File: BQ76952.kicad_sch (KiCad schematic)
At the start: 1 part, among them U3 BQ76952PFBR

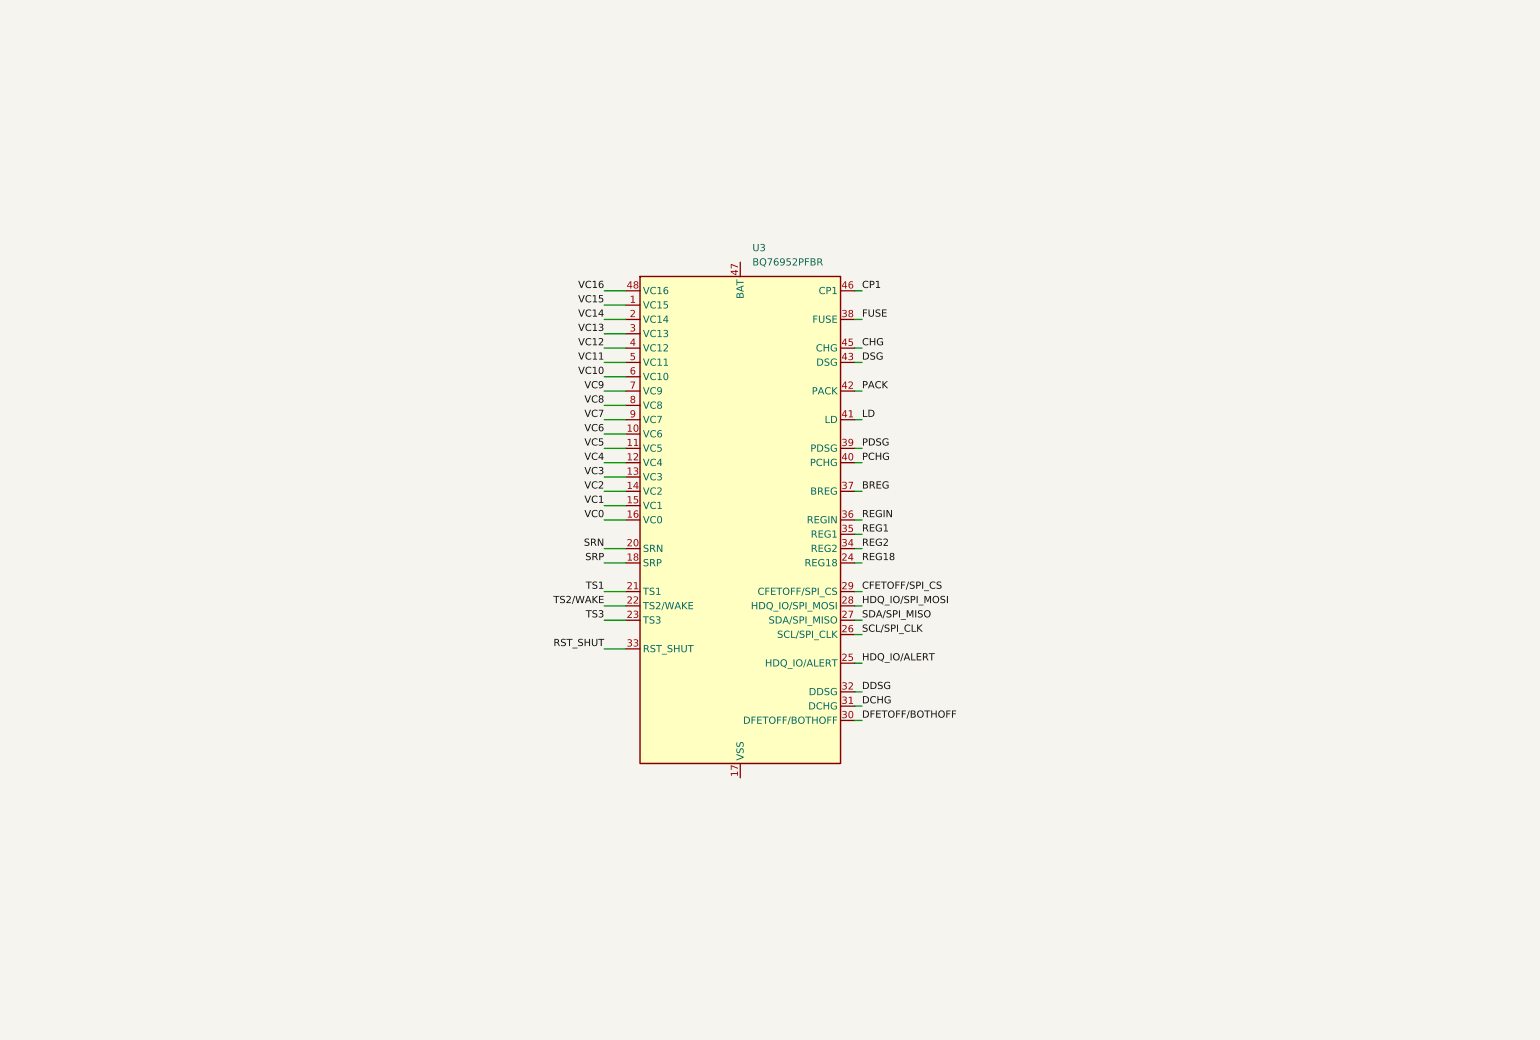
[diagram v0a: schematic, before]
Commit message: Add files via upload
Updated BQ76952 schematic with passive cell balancing, voltage readout to ESP32 and temperature sensing. To do: Connect remaining pins on BQ76952 to ESP32.
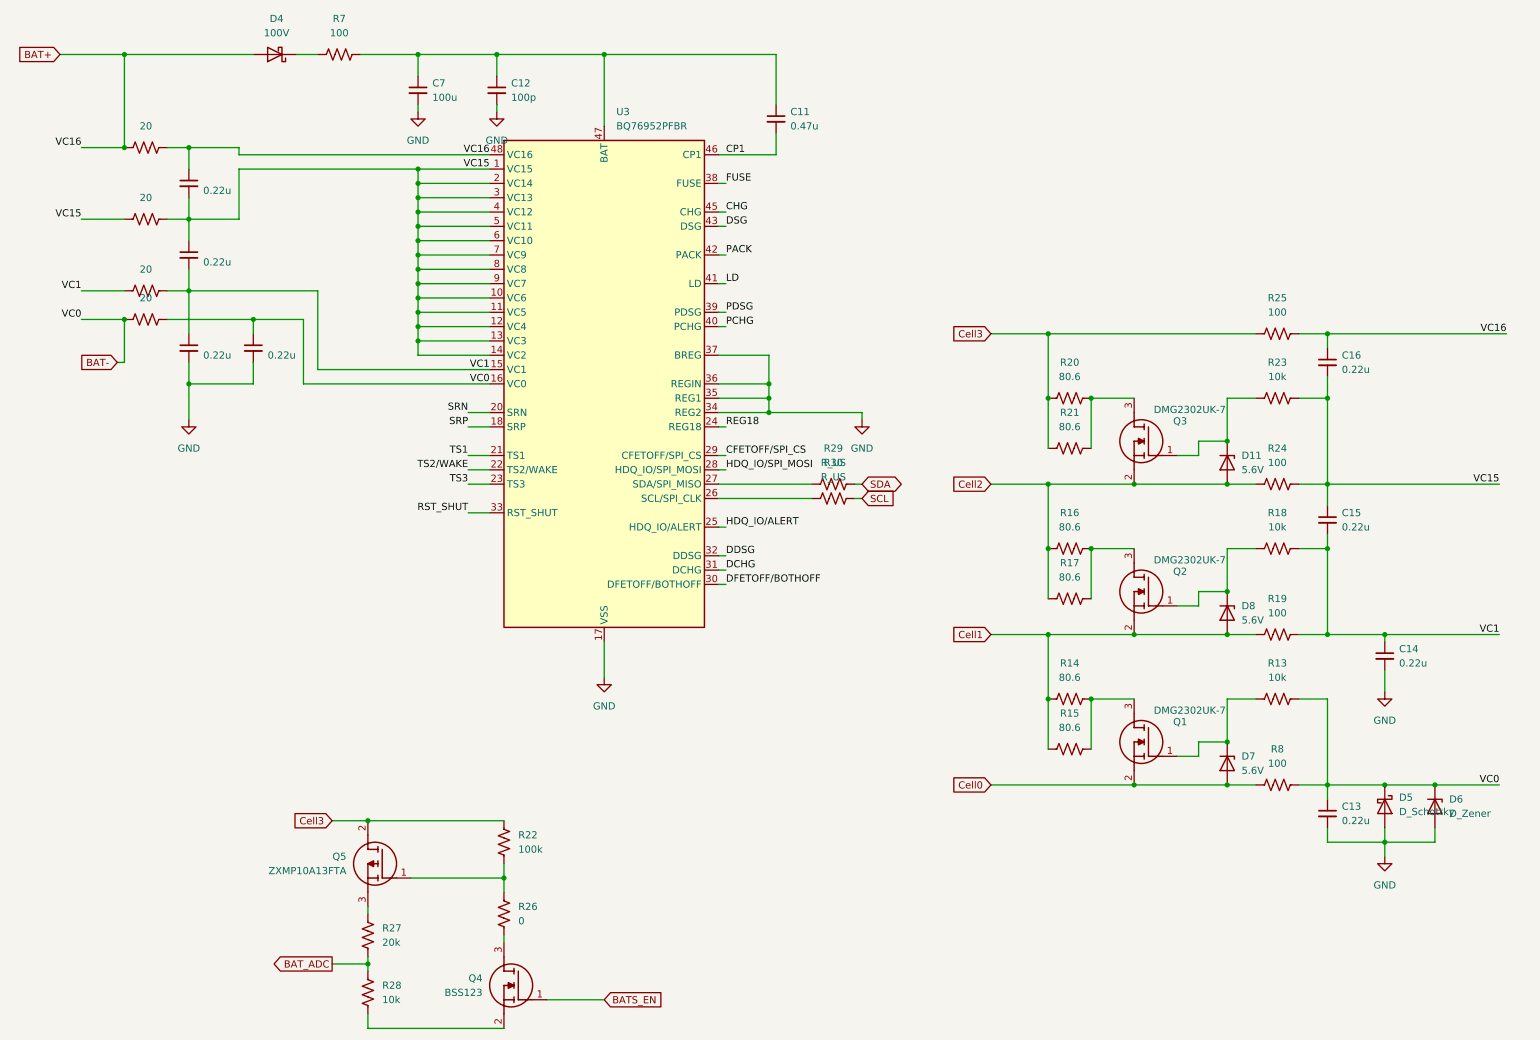
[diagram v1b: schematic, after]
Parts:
- added C10, C13, C14, C15, C16, C6, C8, C9: 0.22u, symbol Device:C_Small
- added C11: 0.47u, symbol Device:C_Small
- added C12: 100p, symbol Device:C_Small
- added C7: 100u, symbol Device:C_Small
- added D11, D7, D8: 5.6V, symbol Device:D_Zener
- added D4: 100V, symbol Device:D_Schottky
- added D5: D_Schottky, symbol Device:D_Schottky
- added D6: D_Zener, symbol Device:D_Zener
- added Q1, Q2, Q3: DMG2302UK-7, SOT96P240X110-3N, symbol SamacSys_Parts:DMG2302UK-7
- added Q4: BSS123, SOT96P237X111-3N, symbol SamacSys_Parts:BSS123
- added Q5: ZXMP10A13FTA, SOT96P240X110-3N, symbol SamacSys_Parts:ZXMP10A13FTA
- added R10, R11, R12, R9: 20, symbol Device:R_US
- added R13, R18, R23, R28: 10k, symbol Device:R_US
- added R14, R15, R16, R17, R20, R21: 80.6, symbol Device:R_US
- added R19, R24, R25, R7, R8: 100, symbol Device:R_US
- added R22: 100k, symbol Device:R_US
- added R26: 0, symbol Device:R_US
- added R27: 20k, symbol Device:R_US
- added R29, R30: R_US, symbol Device:R_US
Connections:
- net BREG is gone; now on net GND: U3.37 (BREG)
- net REG1 is gone; now on net GND: U3.35 (REG1)
- net REG2 is gone; now on net GND: U3.34 (REG2)
- net REGIN is gone; now on net GND: U3.36 (REGIN)
- net VC10 is gone; now on net VC15: U3.6 (VC10)
- net VC11 is gone; now on net VC15: U3.5 (VC11)
- net VC12 is gone; now on net VC15: U3.4 (VC12)
- net VC13 is gone; now on net VC15: U3.3 (VC13)
- net VC14 is gone; now on net VC15: U3.2 (VC14)
- net VC2 is gone; now on net VC15: U3.14 (VC2)
- net VC3 is gone; now on net VC15: U3.13 (VC3)
- net VC4 is gone; now on net VC15: U3.12 (VC4)
- net VC5 is gone; now on net VC15: U3.11 (VC5)
- net VC6 is gone; now on net VC15: U3.10 (VC6)
- net VC7 is gone; now on net VC15: U3.9 (VC7)
- net VC8 is gone; now on net VC15: U3.8 (VC8)
- net VC9 is gone; now on net VC15: U3.7 (VC9)
- net CP1: now also C11.2
- net VC1: now also C10.2, C14.1, C15.2, C6.1, R18.1, R19.1, R9.1, R9.2
- net VC15: now also C10.1, C15.1, C16.2, C9.2, R12.1, R12.2, R23.1, R24.1
- net GND: now reaches U3.17 (VSS)
- net GND: now also C12.2, C13.2, C14.2, C6.2, C7.2, C8.2, D5.2 (A), D6.2 (A)
- net at U3.47 (BAT): now also C11.1, C12.1, C7.1, R7.2
- net SCL/SPI_CLK: no longer names the net of U3.26 (SCL/SPI_CLK)
- net SCL/SPI_CLK: now also R30.1
- net SDA/SPI_MISO: no longer names the net of U3.27 (SDA/SPI_MISO)
- net SDA/SPI_MISO: now also R29.1
- net VC0 renamed BAT-
- net BAT-: now also C13.1, C8.1, D5.1 (K), D6.1 (K), R10.1, R10.2, R13.1, R8.1
- net VC16 renamed BAT+
- net BAT+: now also C16.1, C9.1, D4.2 (A), R11.1, R11.2, R25.1
- new net: Q5.3 (S), R27.1
- new net: Q1.3 (D), R14.2, R15.2
- new net: D7.1 (K), Q1.1 (G), R13.2
- new net: D11.1 (K), Q3.1 (G), R23.2
- new net: Q5.1 (G), R22.2, R26.1
- new net: D8.1 (K), Q2.1 (G), R18.2
- new net: Q2.3 (D), R16.2, R17.2
- new net: Q3.3 (D), R20.2, R21.2
- new net: D4.1 (K), R7.1
- new net: Q4.3 (D), R26.2
- new net: Q4.2 (S), R28.2
- new net BATS_EN: Q4.1 (G)
- new net BAT_ADC: R27.2, R28.1
- new net Cell0: D7.2 (A), Q1.2 (S), R8.2
- new net Cell1: D8.2 (A), Q2.2 (S), R14.1, R15.1, R19.2
- new net Cell2: D11.2 (A), Q3.2 (S), R16.1, R17.1, R24.2
- new net Cell3: Q5.2 (D), R20.1, R21.1, R22.1, R25.2
- new net SCL: R30.2
- new net SDA: R29.2
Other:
- moved on the sheet: U3

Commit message: Add files via upload
Finalized BQ76952 Schematic with MOS Protection circuit. Need to add connections from chip to ESP32. Then implement PCB.
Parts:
- added C17, C18, C19, C20: 470pF, symbol Device:C
- added C21: 2.2u, symbol Device:C_Small
- added C22, C30, C31, C32: 100p, symbol Device:C_Small
- added C23, C24, C25: 0.1u, symbol Device:C_Small
- added D10, D9: ESD9B3.3ST5G, Diode_SMD:D_SOD-923, symbol Diode:ESD9B3.3ST5G
- added E1, E2: SparkGap, symbol Device:SparkGap
- added NT1: NetTie_2, symbol Device:NetTie_2
- added R31, R32, R47, R48: R_US, symbol Device:R_US
- added R33: 0.001, symbol Device:R_US
- added RT1, RT2, RT3, RT4: 103AT-2, 103AT2, symbol SamacSys_Parts:103AT-2
- R29, R30: value R_US -> 10k
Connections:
- net REG18: now also C21.1
- net SCL: now also U3.26 (SCL/SPI_CLK), D10.2 (A2), D9.2 (A2), E1.2, E2.2
- net SDA: now also U3.27 (SDA/SPI_MISO)
- net SRN: now also C22.1, C23.1, C24.2, R31.1
- net SRP: now also C22.2, C23.2, C25.2, R32.1
- net TS2/WAKE: now also C30.1
- net VC1: no longer R9.1
- net VC15: no longer R12.1
- net +3V3: now reaches R30.1
- net +3V3: now also R29.1; no longer U3.26 (SCL/SPI_CLK)
- net BAT+ renamed VC16
- net VC16: no longer D4.2 (A), R11.1
- net BAT- renamed VC0
- net VC0: no longer R10.1
- net CFETOFF/SPI_CS renamed TEMP4
- net TEMP4: now also C20.1, RT4.1
- net DFETOFF/BOTHOFF renamed FETOFF
- net FETOFF: now also C32.1, R48.1
- net FUSE renamed VSS
- net VSS: now also C12.2, C13.2, C14.2, C6.2, C7.2, C8.2, D5.2 (A), D6.2 (A), U3.17 (VSS), U3.36 (REGIN), C17.2, C18.2, C19.2, C20.2, C21.2, C24.1, C25.1, C30.2, C31.2, C32.2, NT1.1, R47.2, R48.2, RT1.2, RT2.2, RT3.2, RT4.2
- removed net GND: C12.2, C13.2, C14.2, C6.2, C7.2, C8.2, D5.2 (A), D6.2 (A), U3.17 (VSS), U3.34 (REG2), U3.35 (REG1), U3.36 (REGIN), U3.37 (BREG)
- net HDQ_IO/ALERT renamed ALERT
- net HDQ_IO/SPI_MOSI renamed TEMP3
- net TEMP3: now also C19.1, RT3.1
- net RST_SHUT renamed SHUT
- net SHUT: now also C31.1, R47.1
- net TS1 renamed TEMP1
- net TEMP1: now also C17.1, RT1.1
- net TS3 renamed TEMP2
- net TEMP2: now also C18.1, RT2.1
- new net 0P: NT1.2, R10.1, R31.2, R33.1
- new net 1P: R9.1
- new net 2P: R12.1
- new net 3P: D4.2 (A), R11.1
- new net PGND: D10.1 (A1), D9.1 (A1), E1.1, E2.1, R32.2, R33.2
- no-connect marks 0 -> 3
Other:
- added sheet Protection FET (MOS_Protection.kicad_sch)
- moved on the sheet: C13, C14, C15, C16, D11, D5, D6, D7, D8, Q1, Q2, Q3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

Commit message: REV1 PCB that was sent to production (PCBWAY)
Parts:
- removed C10, C13, C14, C15, C16, C6, C8, C9: 0.22u, symbol Device:C_Small
- removed C7: 100u, symbol Device:C_Small
- removed D11, D7, D8: 5.6V, symbol Device:D_Zener
- removed D5: D_Schottky, symbol Device:D_Schottky
- removed D6: D_Zener, symbol Device:D_Zener
- removed Q1, Q2, Q3: DMG2302UK-7, SOT96P240X110-3N, symbol SamacSys_Parts:DMG2302UK-7
- removed R10, R11, R12, R9: 20, symbol Device:R_US
- removed R13, R18, R23: 10k, symbol Device:R_US
- removed R14, R15, R16, R17, R20, R21: 80.6, symbol Device:R_US
- removed R19, R24, R25, R8: 100, symbol Device:R_US
- added R61: 10k, Resistor_SMD:R_0805_2012Metric, symbol Device:R_US
- added TP15, TP16, TP17, TP18, TP19, TP20, TP21, TP22, TP23, TP24, TP25, TP26, TP27, TP28, TP29, TP30, TP31, TP32, TP33, TP34, TP35, TP36, TP37, TP38, TP39, TP40, TP41, TP42, TP43, TP44: TestPoint, TestPoint:TestPoint_Pad_D1.0mm, symbol Connector:TestPoint
- C11, C12, C17, C18, C19, C20, C21, C22, C23, C24, C25, C30, C31, C32: footprint (none) -> Capacitor_SMD:C_0805_2012Metric
- D4: footprint (none) -> Diode_SMD:D_0805_2012Metric
- E1, E2: footprint (none) -> Jumper:SolderJumper-2_P1.3mm_Open_TrianglePad1.0x1.5mm; now left out of the parts list
- NT1: footprint (none) -> Jumper:SolderJumper-2_P1.3mm_Bridged2Bar_Pad1.0x1.5mm
- Q4: footprint SOT96P237X111-3N -> SamacSys_Parts:SOT96P237X111-3N
- Q5: footprint SOT96P240X110-3N -> SamacSys_Parts:SOT96P240X110-3N
- R22, R26, R27, R28, R29, R30, R7: footprint (none) -> Resistor_SMD:R_0805_2012Metric
- R31, R32: value R_US -> 100; footprint (none) -> Resistor_SMD:R_0805_2012Metric
- R33: footprint (none) -> Resistor_SMD:R_2512_6332Metric
- R47, R48: value R_US -> 10k; footprint (none) -> Resistor_SMD:R_0805_2012Metric
- RT1, RT2, RT3, RT4: footprint 103AT2 -> SamacSys_Parts:103AT2; now left out of the parts list
- U3: now left out of the parts list
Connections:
- net 0P is gone; now on net VC0: NT1.2, R31.2, R33.1
- net VC16 is gone; now on net +BATT: U3.48 (VC16)
- net ALERT: now also TP31.1
- net CHG: now also TP42.1
- net CP1: now also TP44.1
- net DCHG: now also TP33.1
- net DDSG: now also TP32.1
- net DSG: now also TP41.1
- net LD: now also TP39.1
- net PACK: now also TP40.1
- net PCHG: now also TP38.1
- net PDSG: now also TP37.1
- net REG18: now also TP35.1
- net SCL: now also TP30.1
- net SDA: now also TP28.1
- net SHUT: now also TP15.1
- net SRN: now also TP18.1
- net SRP: now also TP17.1
- net TEMP1: now also TP27.1
- net TEMP2: now also TP26.1
- net TEMP3: now also TP25.1
- net TEMP4: now also TP24.1
- net TS2/WAKE: now also TP16.1
- net VC0: now also TP19.1
- net VC1: now also TP20.1
- net VC15: now also TP21.1
- net VSS: now also Q4.2 (S), R28.2, R61.2, TP29.1, TP36.1; no longer U3.38 (FUSE)
- net at C11.1, C12.1, R7.2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: now also TP23.1
- net 3P renamed +BATT
- net +BATT: now also TP22.1
- net FETOFF renamed DFETOFF
- net DFETOFF: now also TP34.1
- new net FUSE: R61.1, TP43.1, U3.38 (FUSE)
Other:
- added sheet External Cell Balancing (External_Cell_Balancing.kicad_sch)
- moved on the sheet: C11, C12, D4, R7

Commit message: These files are for the final report
NOTE:
1. PCB has mixed up nets so many traces going to the BQ76952 are DISCONNECTED.
2. BOTH active and passive balancing are connected in parallel even though only active balancing is supposed to be connected.
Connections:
- net +BATT: no longer TP22.1, U3.48 (VC16)
- new net VC16: TP22.1, U3.48 (VC16)
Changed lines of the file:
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@@
-	)
-	(junction
-		(at 33.02 31.75)
-		(diameter 0)
-		(color 0 0 0 0)
 	)
 	(junction
@@
 	(junction
 		(at 147.32 93.98)
-		(diameter 0)
-		(color 0 0 0 0)
-	)
-	(junction
-		(at 33.02 21.59)
 		(diameter 0)
 		(color 0 0 0 0)
@@
 	(wire
 		(pts
-			(xy 25.4 31.75) (xy 33.02 31.75)
-		)
-		(stroke
-			(width 0)
-			(type default)
-		)
-	)
-	(wire
-		(pts
 			(xy 165.1 81.28) (xy 170.18 81.28)
 		)
@@
 	(wire
 		(pts
-			(xy 20.32 21.59) (xy 33.02 21.59)
-		)
-		(stroke
-			(width 0)
-			(type default)
-		)
-	)
-	(wire
-		(pts
 			(xy 68.58 102.87) (xy 68.58 118.11)
 		)
@@
 	(wire
 		(pts
-			(xy 33.02 21.59) (xy 38.1 21.59)
+			(xy 20.32 21.59) (xy 38.1 21.59)
 		)
 		(stroke
@@
 	(wire
 		(pts
-			(xy 33.02 21.59) (xy 33.02 31.75)
-		)
-		(stroke
-			(width 0)
-			(type default)
-		)
-	)
-	(wire
-		(pts
 			(xy 129.54 173.99) (xy 142.24 173.99)
 		)
@@
 	(wire
 		(pts
-			(xy 33.02 31.75) (xy 49.53 31.75)
-		)
-		(stroke
+			(xy 25.4 31.75) (xy 49.53 31.75)
+		)
+		(stroke
